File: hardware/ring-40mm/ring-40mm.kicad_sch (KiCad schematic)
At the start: 44 parts, among them J1 Conn_01x03, J2 Conn_01x03

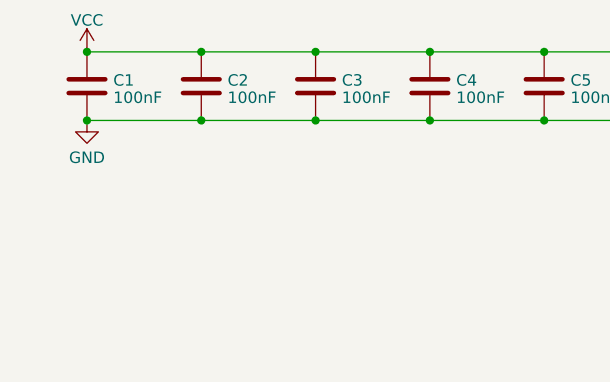
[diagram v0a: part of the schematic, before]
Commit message: ring-40mm: clean up and generate fab files
Change-Id: I3ff063815f256b7ba3f7e43d15cf4eef6ca098e3
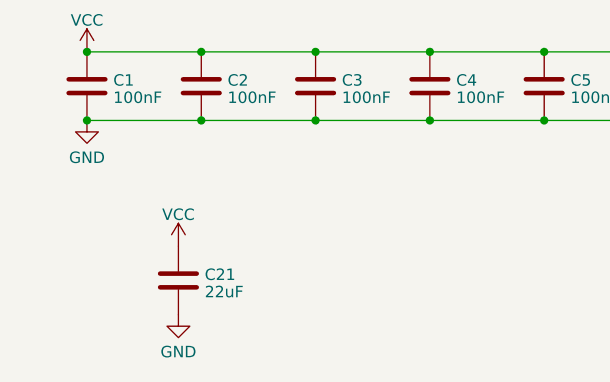
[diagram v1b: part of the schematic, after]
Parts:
- added C21: 22uF, Capacitor_SMD:C_0805_2012Metric, symbol Device:C
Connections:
- net GND: now also C21.2
- net VCC: now also C21.1
